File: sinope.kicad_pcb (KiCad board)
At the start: 2 copper layers, 160 x 103 mm, 47 parts, among them J1 PIOA, J2 SERIAL0, J3 PIOB, J4 SERIAL1, J5 Battery, J6 5VDC, J7 Z80_BUS, Q1 3N3906, SW1 RESET, U1 Z80CPU, U10 MEMORY_GAL, U11 74LS157, U12 TC551001, U2 Z80CTC, U3 Z80PIO, U4 Z80SIO, U5 MAX232, U6 MAX232, U7 IO_GAL, U8 MAX695, U9 27C010, X1 3.6864Mhz

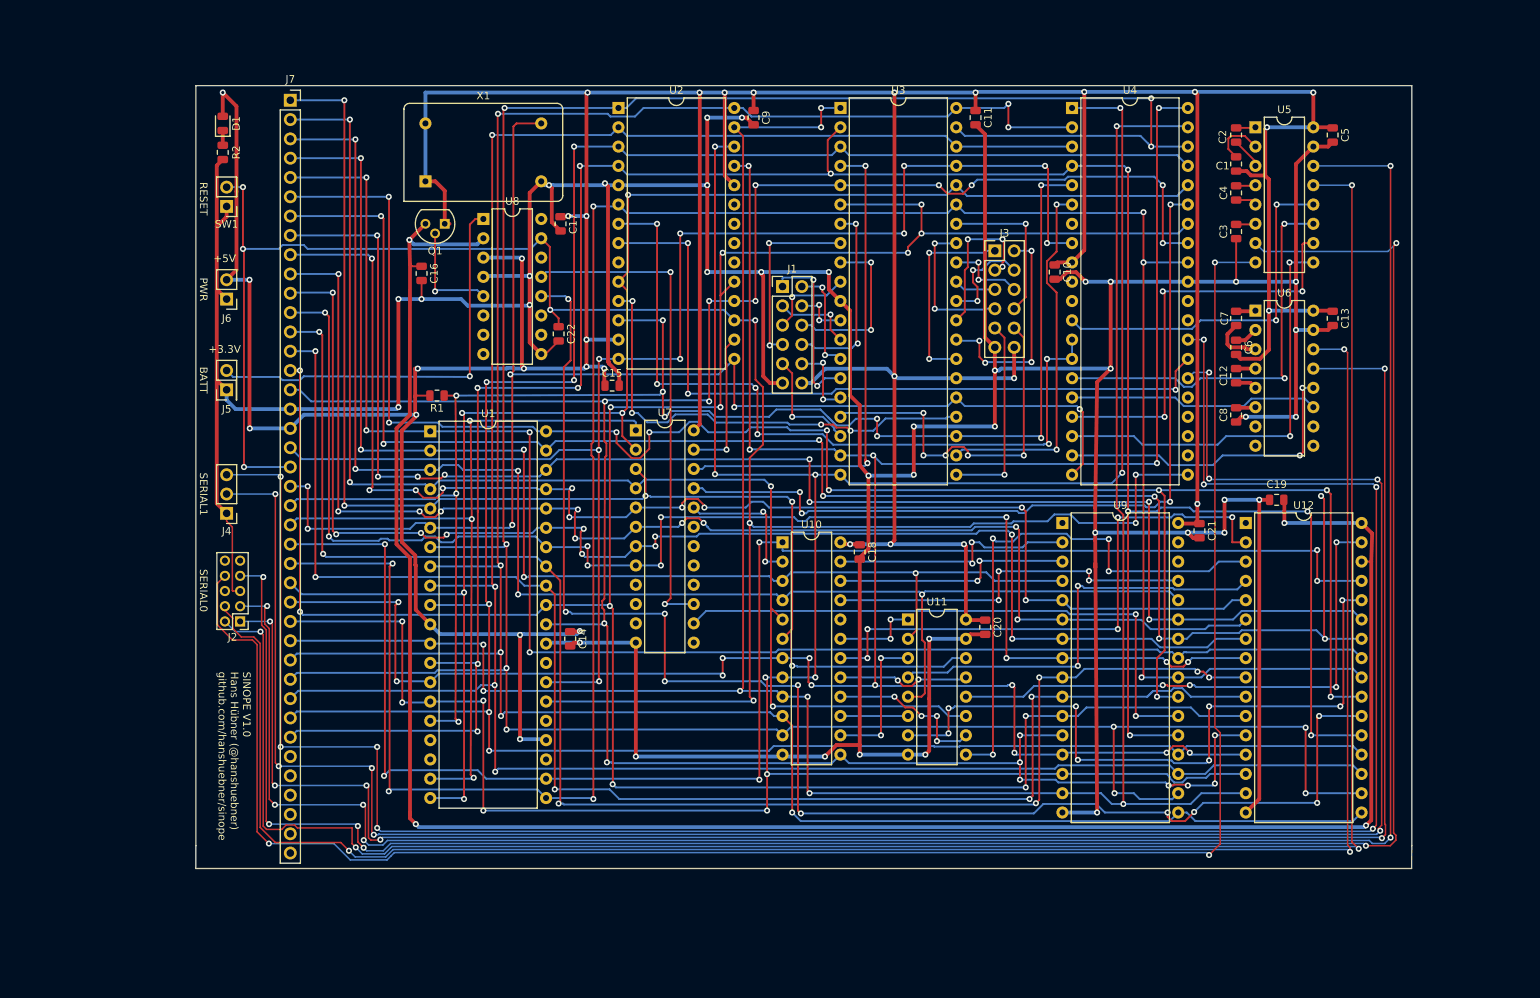
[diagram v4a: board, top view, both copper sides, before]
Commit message: ROM variant jumpers and cleanup, sent to JLCPCB for production
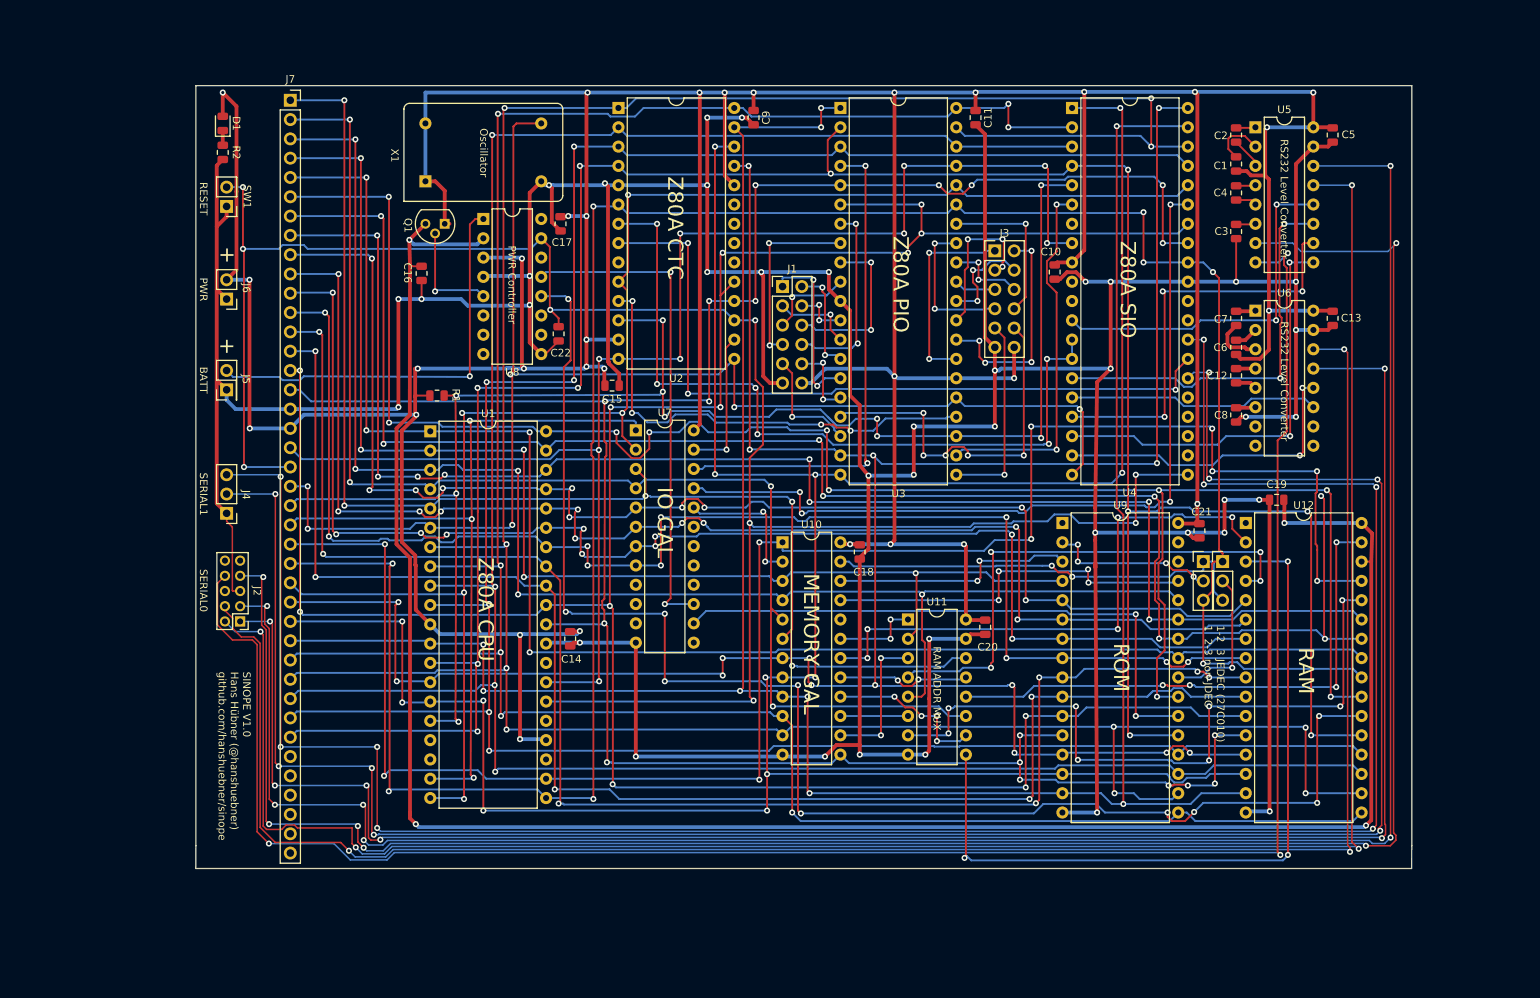
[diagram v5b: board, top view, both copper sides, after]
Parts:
- added JP1: Jumper_3_Bridged12, Connector_PinHeader_2.54mm:PinHeader_1x03_P2.54mm_Vertical, F.Cu at (172.7, 87.6)
- added JP2: Jumper_3_Bridged12, Connector_PinHeader_2.54mm:PinHeader_1x03_P2.54mm_Vertical, F.Cu at (175.3, 87.6)
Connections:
- U9 pad 2: /ROMA16 -> Net-(JP1-Pad2)
- U9 pad 24: ~RD -> Net-(JP2-Pad2)
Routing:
- net ~WR: track 208.9 -> 240.5 mm, vias 6 -> 10
- net Net-(U11-Pad9): track 70.9 -> 101.1 mm, vias 4 -> 3
- net /ROMA16: track 32.8 -> 57.1 mm
- net Net-(JP1-Pad2): track 0.00 -> 22.0 mm, vias 0 -> 4
- net Net-(JP2-Pad2): track 0.00 -> 19.6 mm, vias 0 -> 1
- net Net-(U11-Pad4): track 56.3 -> 68.1 mm, vias 2 -> 4
- net /CTSA: track 249.3 -> 259.4 mm
- net ~RD: track 320.4 -> 315.1 mm, vias 7 -> 8
- net GND: track 747.9 -> 750.3 mm, vias 38 -> 39
- net RAMA16: track 75.5 -> 74.4 mm
- net /A7: track 178.1 -> 178.9 mm
- net /ROMA14: track 49.5 -> 50.3 mm
- net /ROMA15: track 31.9 -> 32.5 mm
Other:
- board text added: "+"
- board text added: "1-2 3 JEDEC (27C010) 1 2-3 non-JDEC"
- board text added: "IO GAL"
- board text added: "MEMORY GAL"
- board text added: "Oscillator"
- board text added: "PWR Controller"
- board text added: "RAM"
- board text added: "RAM ADDR MUX"
- board text added: "ROM"
- board text added: "RS232 Level Converter"
- board text added: "Z80A CPU"
- board text added: "Z80A CTC"
- board text added: "Z80A PIO"
- board text added: "Z80A SIO"
- board text removed: "+3.3V"
- board text removed: "+5V"

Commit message: Begin work on v2
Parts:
- removed C12, C13, C8: 100nF, Capacitor_SMD:C_0805_2012Metric
- removed J5: Battery, Connector_PinHeader_2.54mm:PinHeader_2x01_P2.54mm_Vertical
- removed J6: 5VDC, Connector_PinHeader_2.54mm:PinHeader_1x02_P2.54mm_Vertical
- added BT1: Battery, Battery:Battery_Panasonic_CR2032-VS1N_Vertical_CircularHoles, F.Cu at (77.5, 30.5)
- added D2: LED, LED_SMD:LED_0805_2012Metric, F.Cu at (43.7, 32.8)
- added D3: LED, LED_SMD:LED_0805_2012Metric, F.Cu at (43.7, 41.7)
- added R3: 330, Resistor_SMD:R_0805_2012Metric, F.Cu at (59.7, 26.7)
- added R4: 330, Resistor_SMD:R_0805_2012Metric, F.Cu at (81.9, 53.5)
- added R5: 3k3, Resistor_SMD:R_0805_2012Metric, F.Cu at (78.7, 124.5)
- added R6: 3k3, Resistor_SMD:R_0805_2012Metric, F.Cu at (73.7, 124.5)
- added R7: 3k3, Resistor_SMD:R_0805_2012Metric, F.Cu at (84.2, 124.5)
- J2: value SERIAL0 -> SERIAL1; footprint Connector_PinHeader_2.00mm:PinHeader_2x05_P2.00mm_Vertical -> Connector_PinHeader_2.54mm:PinHeader_2x05_P2.54mm_Vertical
- J4: value SERIAL1 -> USB_B_Micro; footprint Connector_PinHeader_2.54mm:PinHeader_1x03_P2.54mm_Vertical -> Connector_USB:USB_Micro-B_Molex-105017-0001
- J7: footprint Connector_PinSocket_2.54mm:PinSocket_1x40_P2.54mm_Vertical -> Connector_PinSocket_2.54mm:PinSocket_1x39_P2.54mm_Vertical
- JP1, JP2: value Jumper_3_Bridged12 -> SolderJumper_3_Bridged12
- Q1: value 3N3906 -> MMBT3904; footprint Package_TO_SOT_THT:TO-92 -> Package_TO_SOT_SMD:SOT-23
- SW1: footprint Connector_PinHeader_2.54mm:PinHeader_1x02_P2.54mm_Vertical -> Button_Switch_SMD:SW_SPST_PTS645
- U6: value MAX232 -> FT232RL; footprint Package_DIP:DIP-16_W7.62mm -> Package_SO:SSOP-28_5.3x10.2mm_P0.65mm
- moved U6 105.3 mm to (74.4, 49.0)
- moved C7 95.3 mm to (81.9, 50.5), turned to 0 degrees
- moved C6 91.9 mm to (86.4, 44.5), turned to 0 degrees
- moved X1 83.3 mm to (144.8, 74.9)
- moved C1 81.0 mm to (97.0, 48.0)
- moved C2 81.0 mm to (97.0, 44.2)
- moved C3 81.0 mm to (97.0, 56.9)
- moved C4 81.0 mm to (97.0, 51.8)
- moved C5 80.3 mm to (110.5, 44.2)
- moved U5 80.3 mm to (100.3, 43.2)
- moved J1 73.4 mm to (190.5, 57.1)
- moved C9 48.3 mm to (161.8, 27.9)
- moved U2 48.3 mm to (144.0, 26.7)
- moved J3 46.6 mm to (190.5, 35.6)
- moved C11 44.5 mm to (187.2, 27.9)
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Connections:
- net /CTSA renamed Net-(J2-Pad8)
- net /RTSA renamed Net-(J2-Pad7)
- net /RxDA renamed Net-(J2-Pad2)
- net /TxDA renamed Net-(J2-Pad3)
- net Net-(U1-Pad18) renamed ~HALT
- net Net-(U1-Pad23) renamed ~BUSACK
- net Net-(U1-Pad28) renamed ~RFSH
- C6 pad 1: Net-(C6-Pad1) -> +5V
- C6 pad 2: +5V -> GND
- C7 pad 2: Net-(C7-Pad2) -> GND
- J2 pad 1: /DCDA -> Net-(J2-Pad1)
- J2 pad 4: /DTRA -> Net-(J2-Pad4)
- J4 pad 1: GND -> +5V
- J4 pad 2: Net-(J4-Pad2) -> USB_D-
- J4 pad 3: Net-(J4-Pad3) -> USB_D+
- J7 pad 35: Net-(J7-Pad35) -> TxDB
- J7 pad 36: Net-(J7-Pad36) -> RxDB
- J7 pad 37: Net-(J7-Pad37) -> SPARE1
- J7 pad 38: Net-(J7-Pad38) -> SPARE2
- J7 pad 39: Net-(J7-Pad39) -> SPARE3
- JP1 pad 2: Net-(JP1-Pad2) -> /ROMA16
- JP2 pad 2: Net-(JP2-Pad2) -> ~RD
- R1 pad 1: ~INT -> ~WAIT
- U1 pad 17: Net-(U1-Pad17) -> ~NMI
- U1 pad 24: +5V -> ~WAIT
- U1 pad 25: Net-(U1-Pad25) -> ~BUSRQ
- U4 pad 26: Net-(J4-Pad2) -> TxDB
- U4 pad 28: Net-(J4-Pad3) -> RxDB
- U5 pad 10: Net-(U4-Pad17) -> Net-(U4-Pad24)
- U5 pad 11: Net-(U4-Pad15) -> TxDB
- U5 pad 12: Net-(U4-Pad12) -> RxDB
- U5 pad 9: Net-(U4-Pad18) -> Net-(U4-Pad23)
- U6 pad 1: Net-(C7-Pad1) -> Net-(U4-Pad12)
- U6 pad 10: Net-(U6-Pad10) -> Net-(U4-Pad16)
- U6 pad 11: Net-(U4-Pad16) -> Net-(U4-Pad17)
- U6 pad 12: Net-(U4-Pad19) -> Net-(U6-Pad12)
- U6 pad 13: /DCDA -> Net-(U6-Pad13)
- U6 pad 14: /DTRA -> Net-(U6-Pad14)
- U6 pad 15: GND -> USB_D+
- U6 pad 16: +5V -> USB_D-
- U6 pad 2: Net-(C6-Pad1) -> Net-(U4-Pad19)
- U6 pad 3: Net-(C7-Pad2) -> Net-(U4-Pad18)
- U6 pad 4: Net-(C12-Pad2) -> +5V
- U6 pad 5: Net-(C12-Pad1) -> Net-(U4-Pad15)
- U6 pad 7: Net-(U6-Pad7) -> GND
- U6 pad 8: Net-(U6-Pad8) -> (no net)
- U7 pad 17: (no net) -> SPARE3
- U7 pad 18: (no net) -> SPARE2
- U7 pad 19: (no net) -> SPARE1
- U9 pad 2: Net-(JP1-Pad2) -> /ROMA16
- U9 pad 24: Net-(JP2-Pad2) -> ~RD
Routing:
- net GND: track 750.3 -> 0.00 mm, vias 39 -> 0
- net +5V: track 710.7 -> 0.00 mm, vias 32 -> 0
- net /D4: track 384.6 -> 0.00 mm, vias 10 -> 0
- net /D1: track 358.2 -> 0.00 mm, vias 13 -> 0
- net /D7: track 340.8 -> 0.00 mm, vias 11 -> 0
- net /D2: track 336.6 -> 0.00 mm, vias 9 -> 0
- net /A1: track 333.4 -> 0.00 mm, vias 12 -> 0
- net /D0: track 328.0 -> 0.00 mm, vias 16 -> 0
- net /D3: track 324.8 -> 0.00 mm, vias 7 -> 0
- net /D6: track 324.7 -> 0.00 mm, vias 6 -> 0
- net /A0: track 316.1 -> 0.00 mm, vias 18 -> 0
- net ~RD: track 315.1 -> 0.00 mm, vias 8 -> 0
- net /D5: track 313.7 -> 0.00 mm, vias 4 -> 0
- net Net-(J4-Pad3): track 286.9 -> 0.00 mm, vias 8 -> 0
- net Net-(J2-Pad7): track 286.4 -> 0.00 mm, vias 6 -> 0
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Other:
- board size 160 x 103 mm -> 160 x 100 mm
- net class Default: clearance 0.2 -> 0.127; trace_width 0.25 -> 0.127; via_dia 0.8 -> 0.6; via_drill 0.4 -> 0.3
- net class Power added: clearance 0.2, trace_width 0.5, via_dia 0.8, via_drill 0.4
- rule trace_clearance: 0.2 -> 0.127
- rule trace_min: 0.2 -> 0.127
- rule via_min_drill: 0.3 -> 0.2
- rule via_min_size: 0.4 -> 0.45
- board text removed: "+"
- board text removed: "BATT"
- board text removed: "PWR"
- board text removed: "SERIAL0"
- board text removed: "SERIAL1"
